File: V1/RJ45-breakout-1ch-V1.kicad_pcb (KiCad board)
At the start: 2 copper layers, 22.9 x 30.5 mm, 3 parts, among them J1 RJ45, J2 Screw_Terminal_01x04

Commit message: pcb tweaks
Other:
- board text added: "RJ45-BREAKOUT-1CH-V1"
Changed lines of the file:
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@@
     (effects (font (size 1.5 1.2) (thickness 0.2)) (justify mirror))
+  )
+  (gr_text "RJ45-BREAKOUT-1CH-V1" (at 158.496 95.25 90) (layer "B.Cu")
+    (effects (font (size 1.2 1) (thickness 0.2)) (justify mirror))
   )
   (gr_text "SW3" (at 156.21 111.76) (layer "B.Cu")
@@
   )
   (dimension (type aligned) (layer "Dwgs.User")
-    (pts (xy 63.5 101.6) (xy 63.5 132.08))
+    (pts (xy 136.525 83.82) (xy 136.525 114.3))
     (height 2.54)
-    (gr_text "30.4800 mm" (at 59.81 116.84 90) (layer "Dwgs.User")
+    (gr_text "30.4800 mm" (at 132.835 99.06 90) (layer "Dwgs.User")
       (effects (font (size 1 1) (thickness 0.15)))
     )
@@
   )
   (dimension (type aligned) (layer "Dwgs.User")
-    (pts (xy 87.63 100.33) (xy 64.77 100.33))
+    (pts (xy 160.02 83.185) (xy 137.16 83.185))
     (height 2.54)
-    (gr_text "22.8600 mm" (at 76.2 96.64) (layer "Dwgs.User")
+    (gr_text "22.8600 mm" (at 148.59 79.495) (layer "Dwgs.User")
       (effects (font (size 1 1) (thickness 0.15)))
     )

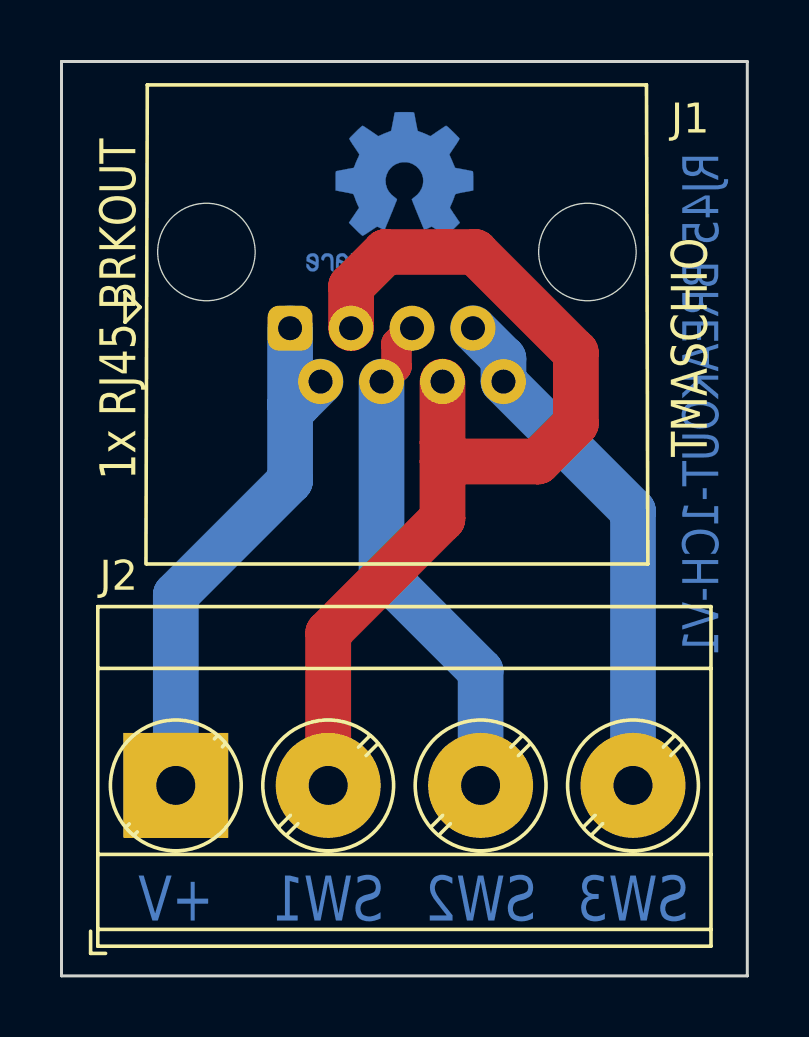
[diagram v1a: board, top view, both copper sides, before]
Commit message: Update RJ45-breakout-1ch-V1.kicad_pcb
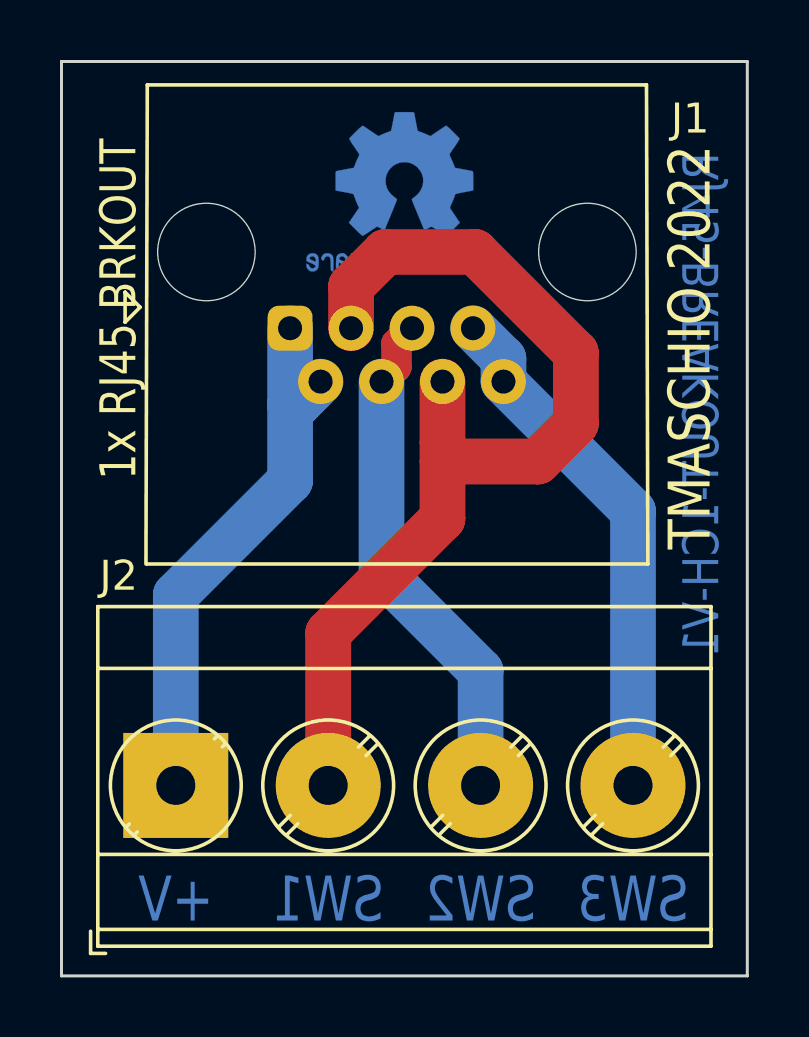
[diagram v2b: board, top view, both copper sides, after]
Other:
- board text added: "TMASCHIO 2022"
- board text removed: "TMASCHIO"
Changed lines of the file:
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@@
     (effects (font (size 1.2 1) (thickness 0.2)))
   )
-  (gr_text "TMASCHIO" (at 158.115 93.345 90) (layer "F.SilkS")
-    (effects (font (size 1.2 1) (thickness 0.2)))
+  (gr_text "TMASCHIO 2022" (at 158.115 93.345 90) (layer "F.SilkS")
+    (effects (font (size 1.4 1.2) (thickness 0.2)))
   )
   (dimension (type aligned) (layer "Dwgs.User")
